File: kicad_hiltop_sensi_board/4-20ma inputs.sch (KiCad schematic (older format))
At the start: 36 parts, among them U16 MAX4194, U19 MAX4194, U20 MAX4194, U21 MAX4194

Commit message: Updated board layout LBBC sensi board
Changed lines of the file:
@@
 Wire Wire Line
 	2750 2450 2750 2400
-$Comp
-L Devtank:+3.3V #PWR0113
-U 1 1 5DE24768
-P 4500 1500
-F 0 "#PWR0113" H 4500 1350 50  0001 C CNN
-F 1 "+3.3V" H 4515 1673 50  0000 C CNN
-F 2 "" H 4500 1500 50  0000 C CNN
-F 3 "" H 4500 1500 50  0000 C CNN
-	1    4500 1500
-	1    0    0    -1
-$EndComp
 Wire Wire Line
 	2750 2050 3550 2050
@@
 Wire Wire Line
 	2750 4650 2750 4600
-$Comp
-L Devtank:+3.3V #PWR0118
-U 1 1 5D781CAC
-P 4500 3700
-F 0 "#PWR0118" H 4500 3550 50  0001 C CNN
-F 1 "+3.3V" H 4515 3873 50  0000 C CNN
-F 2 "" H 4500 3700 50  0000 C CNN
-F 3 "" H 4500 3700 50  0000 C CNN
-	1    4500 3700
-	1    0    0    -1
-$EndComp
 Wire Wire Line
 	2750 4250 3550 4250
@@
 Wire Wire Line
 	6850 2450 6850 2400
-$Comp
-L Devtank:+3.3V #PWR0123
-U 1 1 5D789E6F
-P 8600 1500
-F 0 "#PWR0123" H 8600 1350 50  0001 C CNN
-F 1 "+3.3V" H 8615 1673 50  0000 C CNN
-F 2 "" H 8600 1500 50  0000 C CNN
-F 3 "" H 8600 1500 50  0000 C CNN
-	1    8600 1500
-	1    0    0    -1
-$EndComp
 Wire Wire Line
 	6850 2050 7650 2050
@@
 Wire Wire Line
 	6850 4650 6850 4600
-$Comp
-L Devtank:+3.3V #PWR0128
-U 1 1 5D79139B
-P 8600 3700
-F 0 "#PWR0128" H 8600 3550 50  0001 C CNN
-F 1 "+3.3V" H 8615 3873 50  0000 C CNN
-F 2 "" H 8600 3700 50  0000 C CNN
-F 3 "" H 8600 3700 50  0000 C CNN
-	1    8600 3700
-	1    0    0    -1
-$EndComp
 Wire Wire Line
 	6850 4250 7650 4250
@@
 Text HLabel 9400 4450 2    60   Input ~ 0
 F4op
+$Comp
+L power:+3V3 #PWR?
+U 1 1 5E623C28
+P 4500 1500
+AR Path="/5E623C28" Ref="#PWR?"  Part="1"
+AR Path="/5D6F5943/5E623C28" Ref="#PWR0134"  Part="1"
+F 0 "#PWR0134" H 4500 1350 50  0001 C CNN
+F 1 "+3V3" H 4515 1673 50  0000 C CNN
+F 2 "" H 4500 1500 50  0001 C CNN
+F 3 "" H 4500 1500 50  0001 C CNN
+	1    4500 1500
+	1    0    0    -1
+$EndComp
+$Comp
+L power:+3V3 #PWR?
+U 1 1 5E62CCFE
+P 4500 3700
+AR Path="/5E62CCFE" Ref="#PWR?"  Part="1"
+AR Path="/5D6F5943/5E62CCFE" Ref="#PWR0153"  Part="1"
+F 0 "#PWR0153" H 4500 3550 50  0001 C CNN
+F 1 "+3V3" H 4515 3873 50  0000 C CNN
+F 2 "" H 4500 3700 50  0001 C CNN
+F 3 "" H 4500 3700 50  0001 C CNN
+	1    4500 3700
+	1    0    0    -1
+$EndComp
+$Comp
+L power:+3V3 #PWR?
+U 1 1 5E633E37
+P 8600 1500
+AR Path="/5E633E37" Ref="#PWR?"  Part="1"
+AR Path="/5D6F5943/5E633E37" Ref="#PWR0168"  Part="1"
+F 0 "#PWR0168" H 8600 1350 50  0001 C CNN
+F 1 "+3V3" H 8615 1673 50  0000 C CNN
+F 2 "" H 8600 1500 50  0001 C CNN
+F 3 "" H 8600 1500 50  0001 C CNN
+	1    8600 1500
+	1    0    0    -1
+$EndComp
+$Comp
+L power:+3V3 #PWR?
+U 1 1 5E6405CE
+P 8600 3700
+AR Path="/5E6405CE" Ref="#PWR?"  Part="1"
+AR Path="/5D6F5943/5E6405CE" Ref="#PWR0173"  Part="1"
+F 0 "#PWR0173" H 8600 3550 50  0001 C CNN
+F 1 "+3V3" H 8615 3873 50  0000 C CNN
+F 2 "" H 8600 3700 50  0001 C CNN
+F 3 "" H 8600 3700 50  0001 C CNN
+	1    8600 3700
+	1    0    0    -1
+$EndComp
 $EndSCHEMATC

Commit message: Sensi board updated pin map
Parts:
- C40, C41, C48, C49: footprint Capacitor_SMD:C_0603_1608Metric -> Capacitor_SMD:C_0402_1005Metric
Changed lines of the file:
@@
 F 0 "C40" V 4548 1850 50  0000 C CNN
 F 1 "0.1uF" V 4639 1850 50  0000 C CNN
-F 2 "Capacitor_SMD:C_0603_1608Metric" H 4838 1700 50  0001 C CNN
+F 2 "Capacitor_SMD:C_0402_1005Metric" H 4838 1700 50  0001 C CNN
 F 3 "" H 4800 1850 50  0001 C CNN
 	1    4800 1850
@@
 F 0 "C41" V 4548 4050 50  0000 C CNN
 F 1 "0.1uF" V 4639 4050 50  0000 C CNN
-F 2 "Capacitor_SMD:C_0603_1608Metric" H 4838 3900 50  0001 C CNN
+F 2 "Capacitor_SMD:C_0402_1005Metric" H 4838 3900 50  0001 C CNN
 F 3 "" H 4800 4050 50  0001 C CNN
 	1    4800 4050
@@
 F 0 "C48" V 8648 1850 50  0000 C CNN
 F 1 "0.1uF" V 8739 1850 50  0000 C CNN
-F 2 "Capacitor_SMD:C_0603_1608Metric" H 8938 1700 50  0001 C CNN
+F 2 "Capacitor_SMD:C_0402_1005Metric" H 8938 1700 50  0001 C CNN
 F 3 "" H 8900 1850 50  0001 C CNN
 	1    8900 1850
@@
 F 0 "C49" V 8648 4050 50  0000 C CNN
 F 1 "0.1uF" V 8739 4050 50  0000 C CNN
-F 2 "Capacitor_SMD:C_0603_1608Metric" H 8938 3900 50  0001 C CNN
+F 2 "Capacitor_SMD:C_0402_1005Metric" H 8938 3900 50  0001 C CNN
 F 3 "" H 8900 4050 50  0001 C CNN
 	1    8900 4050

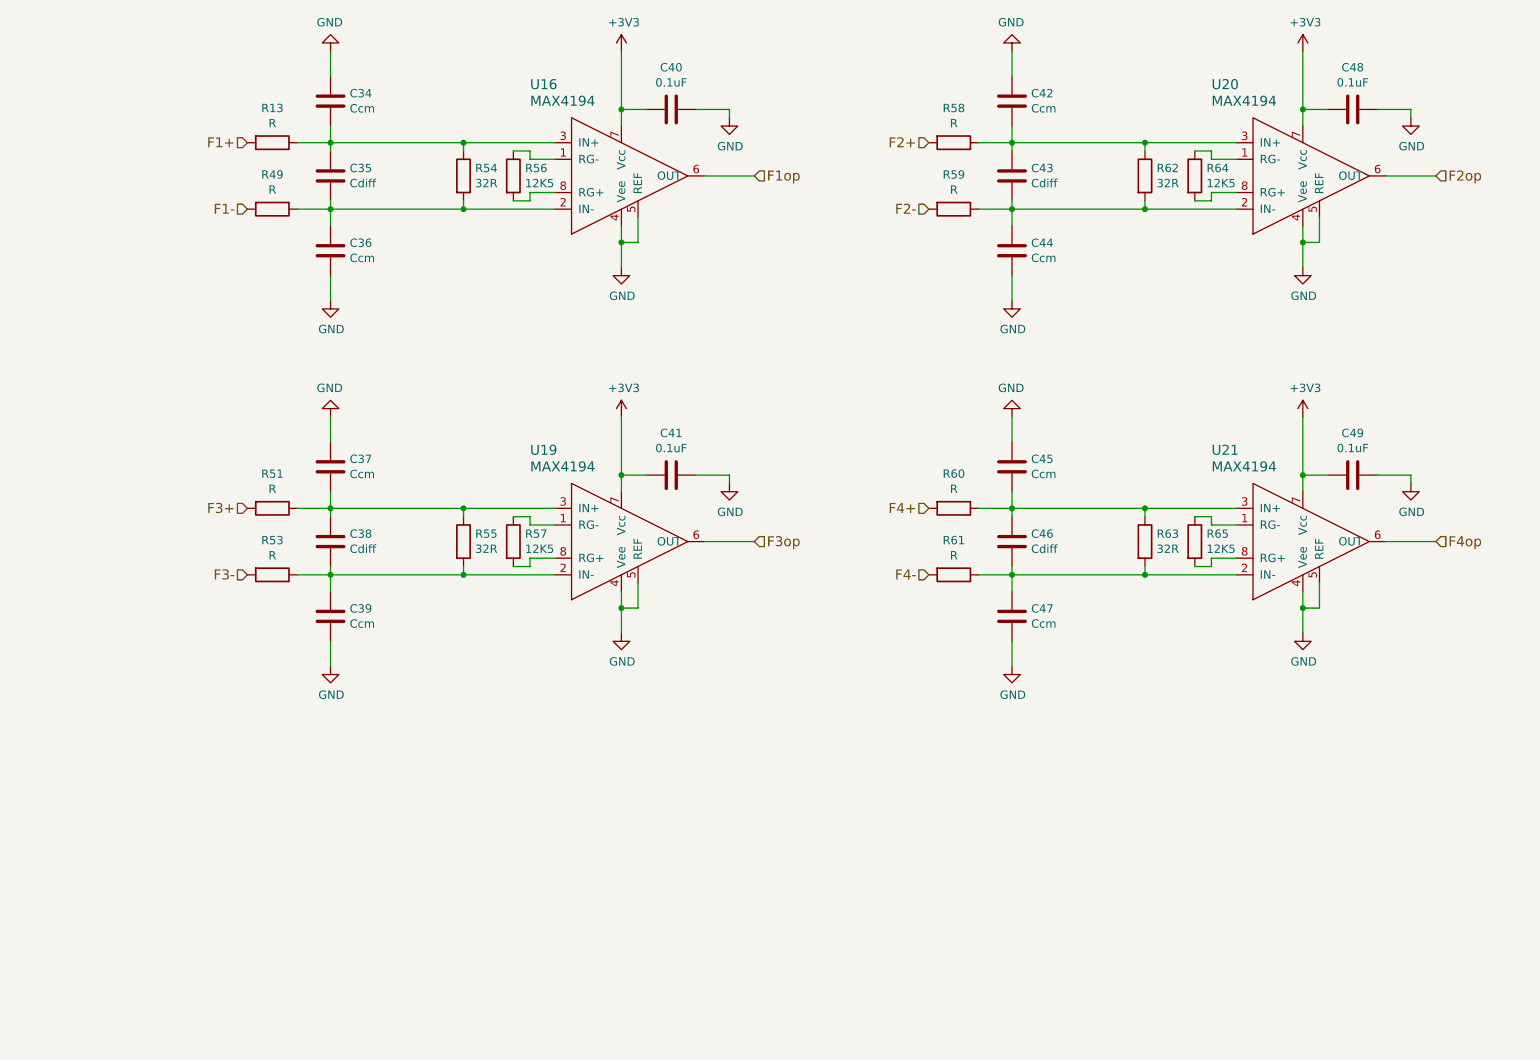
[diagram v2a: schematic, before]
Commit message: Updated sensi board pin map and layout before PCB tracking
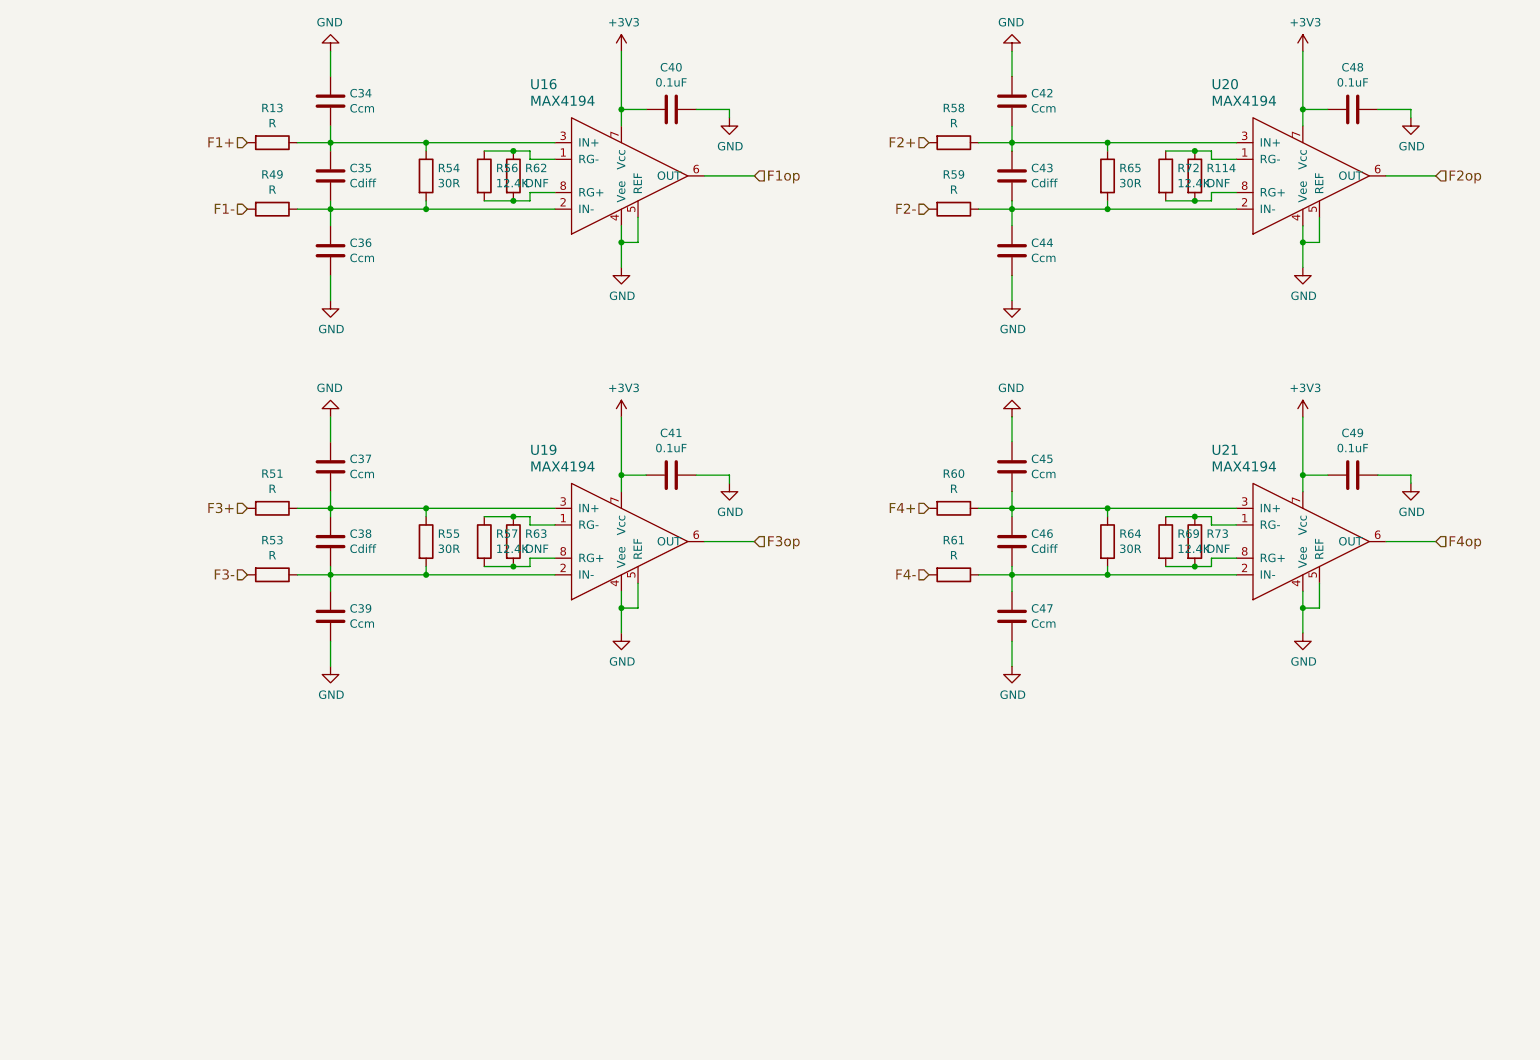
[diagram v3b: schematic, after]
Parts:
- added R114, R73: DNF, Resistor_SMD:R_0603_1608Metric, symbol device:R
- added R69, R72: 12.4K, Resistor_SMD:R_0603_1608Metric, symbol device:R
- C40, C41, C48, C49: Devtank (none) -> 105-019
- R54, R55: value 32R -> 30R; Devtank (none) -> 101-054
- R56, R57: value 12K5 -> 12.4K; footprint Resistor_SMD:R_0402_1005Metric -> Resistor_SMD:R_0603_1608Metric; Devtank (none) -> 103-003
- R62, R63: value 32R -> DNF; Tolerance (none) -> 0.1%
- R64, R65: value 12K5 -> 30R; footprint Resistor_SMD:R_0402_1005Metric -> Resistor_SMD:R_0603_1608Metric; Devtank (none) -> 101-054
- U16, U19, U20, U21: Devtank (none) -> 120-005
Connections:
- net at R56.1, U16.1 (RG-): now also R62.1
- net at R56.2, U16.8 (RG+): now also R62.2
- net at R57.1, U19.1 (RG-): now also R63.1
- net at R57.2, U19.8 (RG+): now also R63.2
- net at U20.1 (RG-): now also R114.1, R72.1; no longer R64.1
- net at C43.2, C44.1, R59.1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: now also R65.2; no longer R62.2
- net at C42.2, C43.1, R58.1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: now also R65.1; no longer R62.1
- net at U20.8 (RG+): now also R114.2, R72.2; no longer R64.2
- net at U21.1 (RG-): now also R69.1, R73.1; no longer R65.1
- net at C46.2, C47.1, R61.1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: now also R64.2; no longer R63.2
- net at C45.2, C46.1, R60.1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: now also R64.1; no longer R63.1
- net at U21.8 (RG+): now also R69.2, R73.2; no longer R65.2
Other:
- moved on the sheet: R54

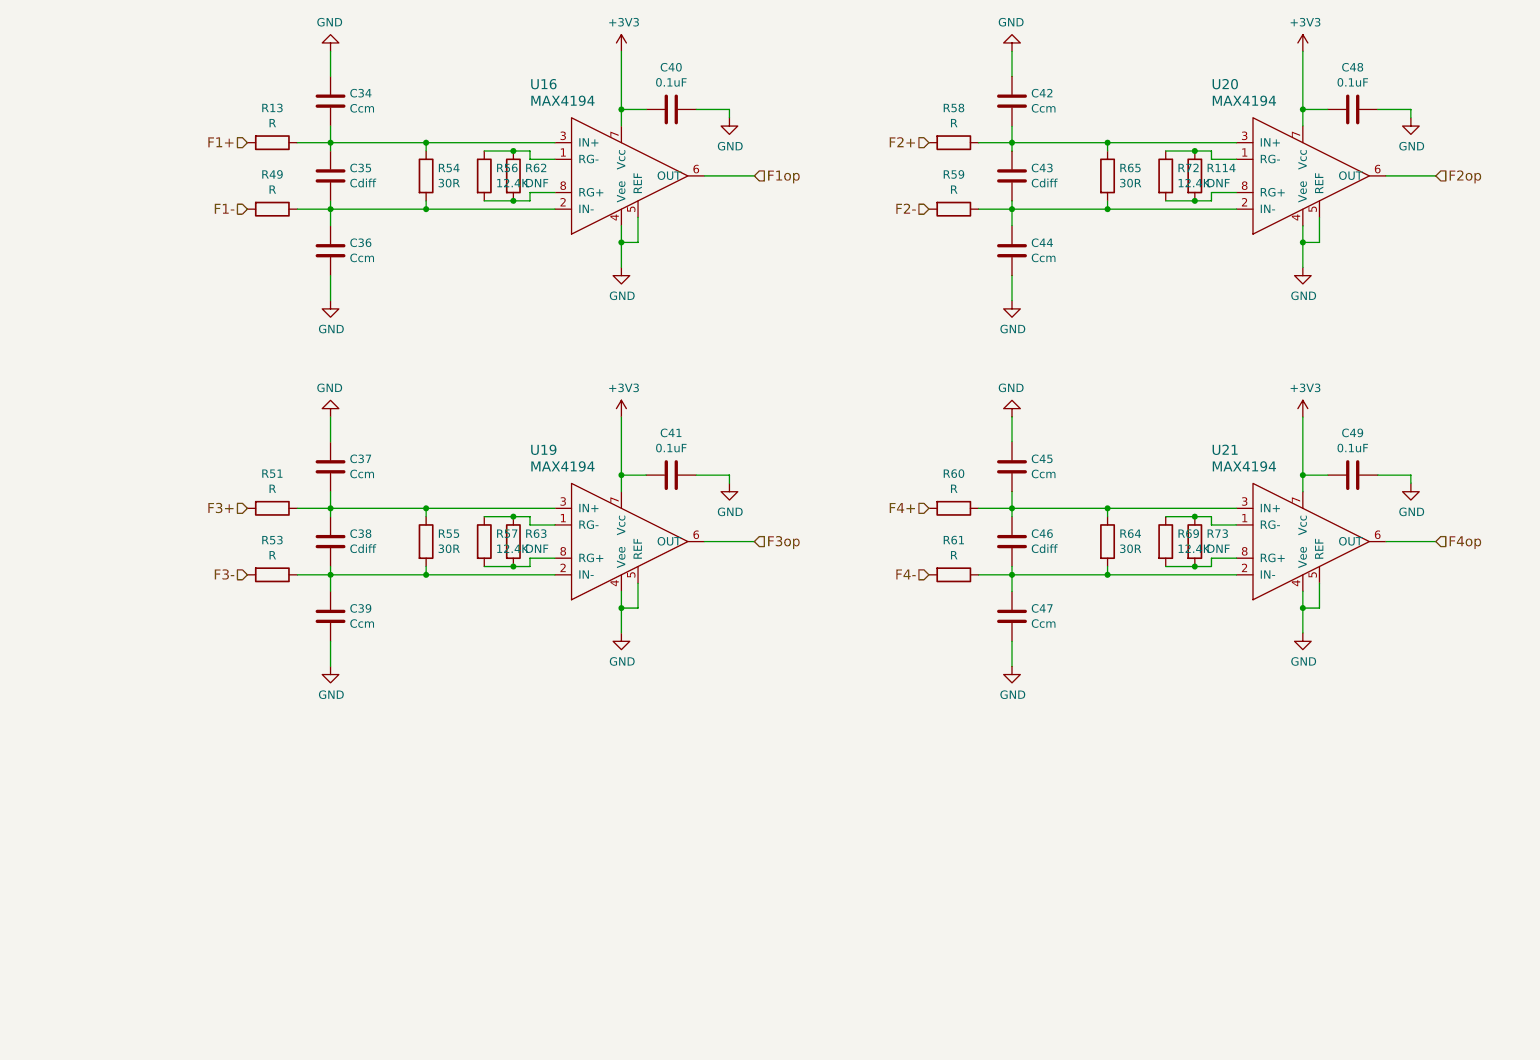
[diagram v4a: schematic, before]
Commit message: Changes to Sensi board after review
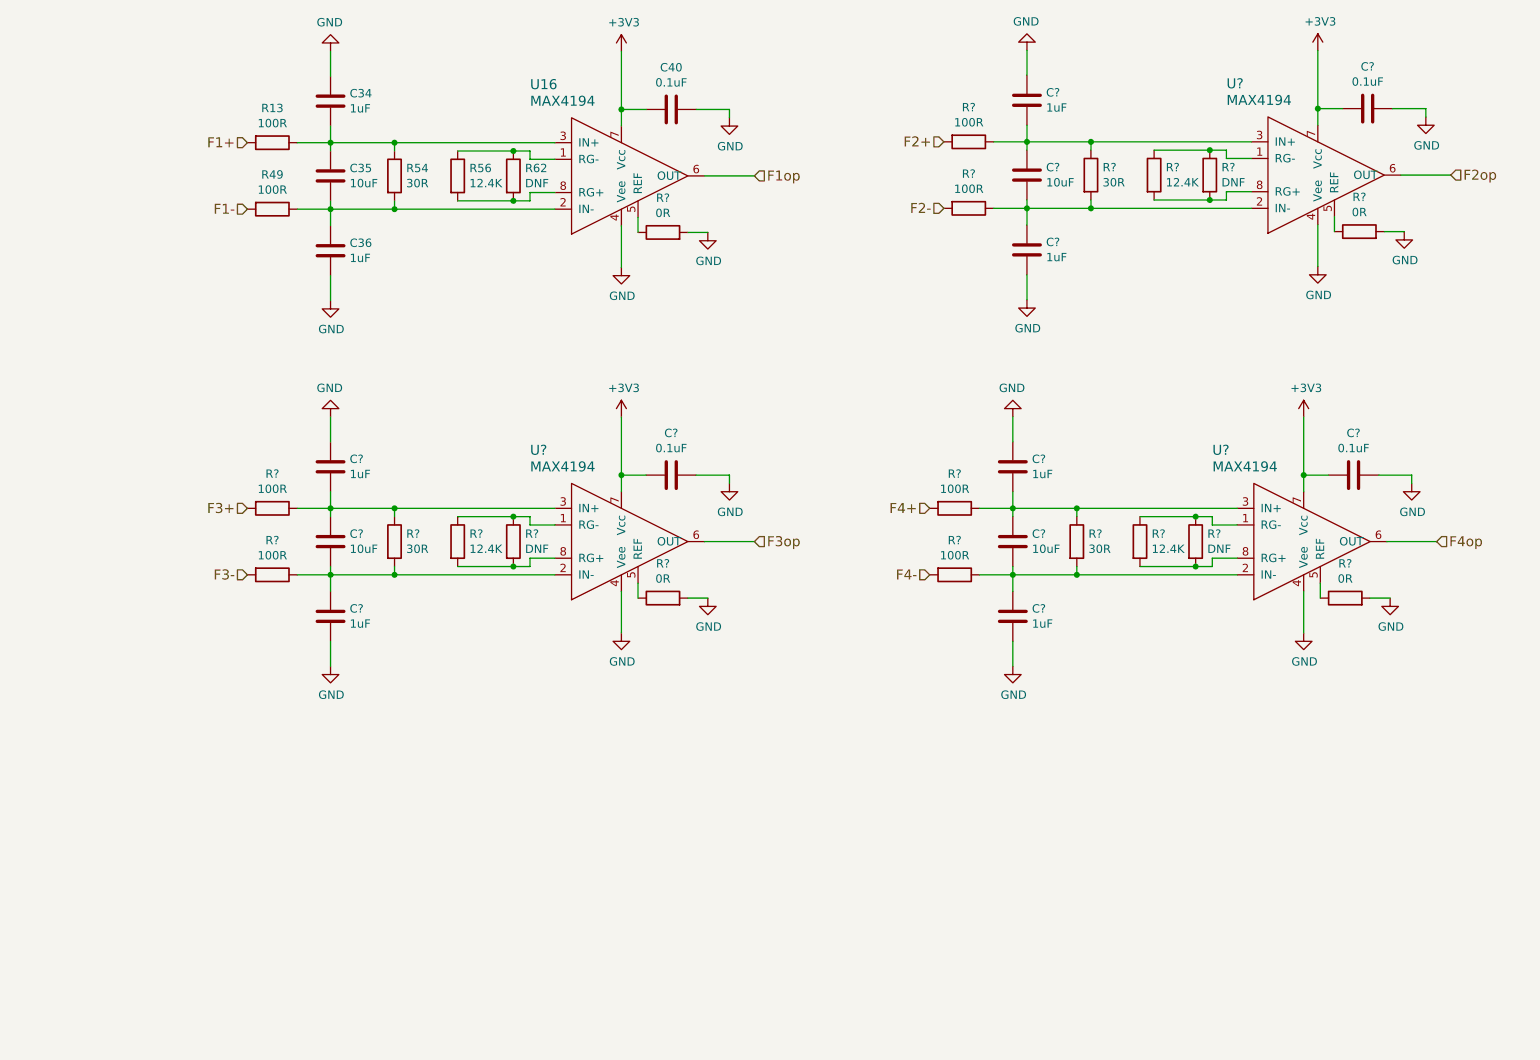
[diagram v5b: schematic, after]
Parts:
- removed C37, C39, C42, C44, C45, C47: Ccm, Capacitor_SMD:C_0603_1608Metric, symbol device:C
- removed C38, C43, C46: Cdiff, Capacitor_SMD:C_0603_1608Metric, symbol device:C
- removed C41, C48, C49: 0.1uF, Capacitor_SMD:C_0402_1005Metric, symbol device:C
- removed R114, R63, R73: DNF, Resistor_SMD:R_0603_1608Metric, symbol device:R
- removed R51, R53, R58, R59, R60, R61: R, Resistor_SMD:R_0603_1608Metric, symbol device:R
- removed R55, R64, R65: 30R, Resistor_SMD:R_0603_1608Metric, symbol device:R
- removed R57, R69, R72: 12.4K, Resistor_SMD:R_0603_1608Metric, symbol device:R
- removed U19, U20, U21: MAX4194, Package_SO:SOIC-8_3.9x4.9mm_P1.27mm, symbol Sensi_Board-rescue:MAX4194-Devtank
- added C? (x3): 0.1uF, Capacitor_SMD:C_0402_1005Metric, symbol device:C
- added C? (x3): 10uF, Capacitor_SMD:C_0603_1608Metric, symbol device:C
- added C? (x6): 1uF, Capacitor_SMD:C_0603_1608Metric, symbol device:C
- added R? (x4): 0R, symbol device:R
- added R? (x6): 100R, Resistor_SMD:R_0603_1608Metric, symbol device:R
- added R? (x3): 30R, Resistor_SMD:R_0603_1608Metric, symbol device:R
- added R? (x3): DNF, Resistor_SMD:R_0603_1608Metric, symbol device:R
- added R? (x3): 12.4K, Resistor_SMD:R_0603_1608Metric, symbol device:R
- added U? (x3): MAX4194, Package_SO:SOIC-8_3.9x4.9mm_P1.27mm, symbol Sensi_Board-rescue:MAX4194-Devtank
- C34, C36: value Ccm -> 1uF
- C35: value Cdiff -> 10uF
- R13, R49: value R -> 100R
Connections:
- net +3V3: now also C?.2, C?.2, C?.2, U?.7 (Vcc), U?.7 (Vcc), U?.7 (Vcc)
- net F2+: now also R?.2
- net F2-: now also R?.2
- net F2op: now also U?.6 (OUT)
- net F3+: now also R?.2
- net F3-: now also R?.2
- net F3op: now also U?.6 (OUT)
- net F4+: now also R?.2
- net F4-: now also R?.2
- net F4op: now also U?.6 (OUT)
- net GND: now also C?.1, C?.1, C?.1, C?.1, C?.1, C?.1, C?.2, C?.2, C?.2, R?.2, R?.2, R?.2, R?.2, U?.4 (Vee), U?.4 (Vee), U?.4 (Vee); no longer U16.5 (REF)
- new net: R?.1, U16.5 (REF)
- new net: R?.1, R?.1, U?.1 (RG-) (x3)
- new net: C?.1, C?.2, R?.1, R?.2, U?.2 (IN-) (x3)
- new net: C?.1, C?.2, R?.1, R?.1, U?.3 (IN+) (x3)
- new net: R?.1, U?.5 (REF) (x3)
- new net: R?.2, R?.2, U?.8 (RG+) (x3)
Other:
- moved on the sheet: R54, R56
